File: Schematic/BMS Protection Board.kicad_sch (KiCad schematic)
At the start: 292 parts, among them J5 Conn_01x04, J6 Conn_01x04, J7 USB_C_Receptacle_USB2.0_14P, Q1 DMN2004K, Q10 ZXMP10A13F, Q11 BSS123, Q12 ZXMP10A13F, Q13 BSS123, Q14 BCX56, Q2 DMN2004K, Q3 DMN2004K, Q4 CSD19531Q5A, Q5 CSD19531Q5A, Q6 ZXMP10A13F, Q7 CSD19531Q5A, Q8 CSD19531Q5A, Q9 BSS123, SW2 SW_Push, U1 1043, U10 TVS2200DRV, U11 BQ76200PW, U12 TLV75533PDBV, U13 BQ78350DBT-R1A, U14 TPD1E05U06DYA, U15 TPD1E05U06DYA, U16 BQ25798RQMR, U2 1043, U22 1043, U23 1043, U24 1043, U25 1043, U26 1043, U27 1043, U28 TPS566238PRQFR, U3 1043, U4 1043, U5 1043, U6 1043, U7 CAT24C512WI-GT3, U8 BQ7692000PWR, U9 TPS25751DREFR

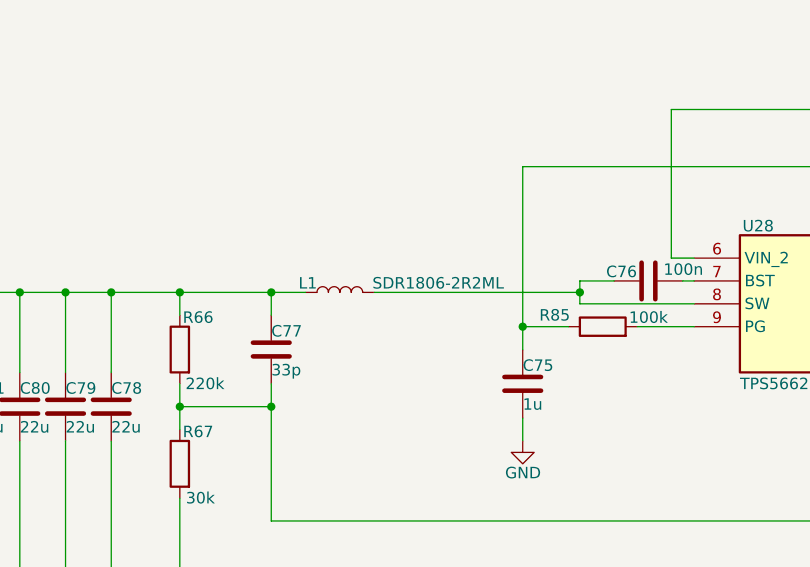
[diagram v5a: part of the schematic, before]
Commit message: Added 6V Line
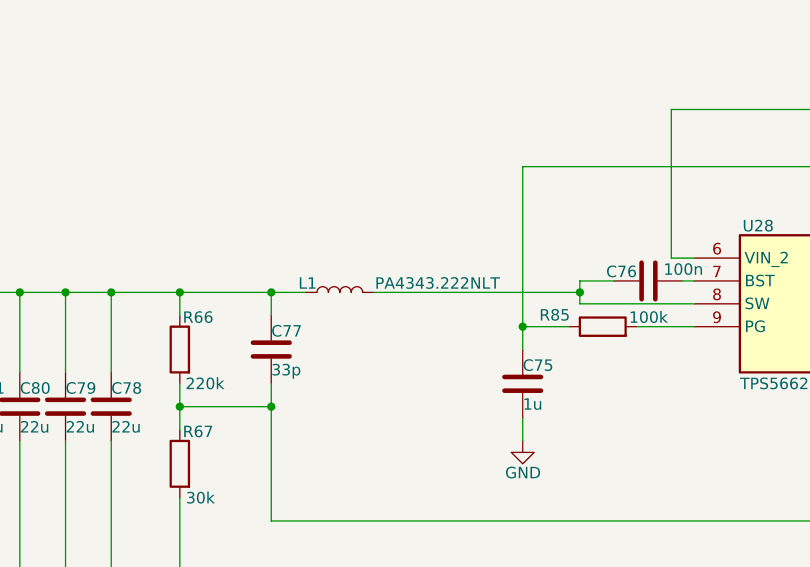
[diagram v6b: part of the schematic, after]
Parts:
- removed L1: SDR1806-2R2ML, SDR1806-2R2ML:SDR18062R2ML, symbol SDR1806-2R2ML:SDR1806-2R2ML
- added L1: PA4343.222NLT, INDPM135125X650N, symbol PA4343.222NLT:PA4343.222NLT
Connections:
- net P5V0: now also L1.1
- net at C76.1, U28.8 (SW): now also L1.2
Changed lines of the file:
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@@
 	)
 	(symbol
-		(lib_id "SDR1806-2R2ML:SDR1806-2R2ML")
-		(at 438.785 412.115 0)
-		(unit 1)
-		(exclude_from_sim no)
-		(in_bom yes)
-		(on_board yes)
-		(dnp no)
-		(property "Reference" "L1"
-			(at 440.944 411.734 0)
-			(effects
-				(font
-					(size 1.27 1.27)
-				)
-			)
-		)
-		(property "Value" "SDR1806-2R2ML"
-			(at 455.422 411.734 0)
-			(effects
-				(font
-					(size 1.27 1.27)
-				)
-			)
-		)
-		(property "Footprint" "SDR1806-2R2ML:SDR18062R2ML"
-			(at 455.295 508.305 0)
-			(effects
-				(font
-					(size 1.27 1.27)
-				)
-				(justify left top)
-				(hide yes)
-			)
-		)
-		(property "Datasheet" "https://www.bourns.com/docs/Product-Datasheets/SDR1806.pdf"
-			(at 455.295 608.305 0)
-			(effects
-				(font
-					(size 1.27 1.27)
-				)
-				(justify left top)
-				(hide yes)
-			)
-		)
-		(property "Description" "Power Inductors - SMD 2.2uH 20% SMD 1806"
-			(at 438.785 412.115 0)
-			(effects
-				(font
-					(size 1.27 1.27)
-				)
-				(hide yes)
-			)
-		)
-		(property "Height" "6.9"
-			(at 455.295 808.305 0)
-			(effects
-				(font
-					(size 1.27 1.27)
-				)
-				(justify left top)
-				(hide yes)
-			)
-		)
-		(property "Mouser Part Number" "652-SDR1806-2R2ML"
-			(at 455.295 908.305 0)
-			(effects
-				(font
-					(size 1.27 1.27)
-				)
-				(justify left top)
-				(hide yes)
-			)
-		)
-		(property "Mouser Price/Stock" "https://www.mouser.co.uk/ProductDetail/Bourns/SDR1806-2R2ML?qs=xrpI9KL%2FXvsM6NNo6hRSNQ%3D%3D"
-			(at 455.295 1008.305 0)
-			(effects
-				(font
-					(size 1.27 1.27)
-				)
-				(justify left top)
-				(hide yes)
-			)
-		)
-		(property "Manufacturer_Name" "Bourns"
-			(at 455.295 1108.305 0)
-			(effects
-				(font
-					(size 1.27 1.27)
-				)
-				(justify left top)
-				(hide yes)
-			)
-		)
-		(property "Manufacturer_Part_Number" "SDR1806-2R2ML"
-			(at 455.295 1208.305 0)
-			(effects
-				(font
-					(size 1.27 1.27)
-				)
-				(justify left top)
-				(hide yes)
-			)
-		)
-		(property "Availability" ""
-			(at 438.785 412.115 0)
-			(effects
-				(font
-					(size 1.27 1.27)
-				)
-				(hide yes)
-			)
-		)
-		(property "Check_prices" ""
-			(at 438.785 412.115 0)
-			(effects
-				(font
-					(size 1.27 1.27)
-				)
-				(hide yes)
-			)
-		)
-		(property "Description_1" ""
-			(at 438.785 412.115 0)
-			(effects
-				(font
-					(size 1.27 1.27)
-				)
-				(hide yes)
-			)
-		)
-		(property "MANUFACTURER" ""
-			(at 438.785 412.115 0)
-			(effects
-				(font
-					(size 1.27 1.27)
-				)
-				(hide yes)
-			)
-		)
-		(property "MAXIMUM_PACKAGE_HEIGHT" ""
-			(at 438.785 412.115 0)
-			(effects
-				(font
-					(size 1.27 1.27)
-				)
-				(hide yes)
-			)
-		)
-		(property "MF" ""
-			(at 438.785 412.115 0)
-			(effects
-				(font
-					(size 1.27 1.27)
-				)
-				(hide yes)
-			)
-		)
-		(property "MP" ""
-			(at 438.785 412.115 0)
-			(effects
-				(font
-					(size 1.27 1.27)
-				)
-				(hide yes)
-			)
-		)
-		(property "PARTREV" ""
-			(at 438.785 412.115 0)
-			(effects
-				(font
-					(size 1.27 1.27)
-				)
-				(hide yes)
-			)
-		)
-		(property "Package" ""
-			(at 438.785 412.115 0)
-			(effects
-				(font
-					(size 1.27 1.27)
-				)
-				(hide yes)
-			)
-		)
-		(property "Part Number" ""
-			(at 438.785 412.115 0)
-			(effects
-				(font
-					(size 1.27 1.27)
-				)
-				(hide yes)
-			)
-		)
-		(property "STANDARD" ""
-			(at 438.785 412.115 0)
-			(effects
-				(font
-					(size 1.27 1.27)
-				)
-				(hide yes)
-			)
-		)
-		(property "SnapEDA_Link" ""
-			(at 438.785 412.115 0)
-			(effects
-				(font
-					(size 1.27 1.27)
-				)
-				(hide yes)
-			)
-		)
-		(property "Specifications" ""
-			(at 438.785 412.115 0)
-			(effects
-				(font
-					(size 1.27 1.27)
-				)
-				(hide yes)
-			)
-		)
-		(pin "1"
-		)
-		(pin "2"
-		)
-		(instances
-			(project ""
-				(path "/fc8533bc-25dd-4c20-9b4c-ffebebd6739b/e8da5d81-614b-4fe5-84b3-4c351fab7114"
-					(reference "L1")
-					(unit 1)
-				)
-			)
-		)
-	)
-	(symbol
 		(lib_id "Device:R")
 		(at 135.89 168.91 90)
@@
 					(unit 1)
 				)
+			)
+		)
+	)
+	(symbol
+		(lib_id "PA4343.222NLT:PA4343.222NLT")
+		(at 444.5 412.75 90)
+		(unit 1)
+		(exclude_from_sim no)
+		(in_bom yes)
+		(on_board yes)
+		(dnp no)
+		(property "Reference" "L1"
+			(at 441.96 412.496 90)
+			(effects
+				(font
+					(size 1.27 1.27)
+				)
+				(justify left top)
+			)
+		)
+		(property "Value" "PA4343.222NLT"
+			(at 462.28 412.496 90)
+			(effects
+				(font
+					(size 1.27 1.27)
+				)
+				(justify left top)
+			)
+		)
+		(property "Footprint" "INDPM135125X650N"
+			(at 540.69 396.24 0)
+			(effects
+				(font
+					(size 1.27 1.27)
+				)
+				(justify left top)
+				(hide yes)
+			)
+		)
+		(property "Datasheet" "https://productfinder.pulseelectronics.com/api/open/part-attachments/datasheet/PA4343.222NLT"
+			(at 640.69 396.24 0)
+			(effects
+				(font
+					(size 1.27 1.27)
+				)
+				(justify left top)
+				(hide yes)
+			)
+		)
+		(property "Description" "Power Inductors - SMD 2.2uH 22A 6.5mm 20% Low Prof"
+			(at 444.5 412.75 0)
+			(effects
+				(font
+					(size 1.27 1.27)
+				)
+				(hide yes)
+			)
+		)
+		(property "Height" "6.5"
+			(at 840.69 396.24 0)
+			(effects
+				(font
+					(size 1.27 1.27)
+				)
+				(justify left top)
+				(hide yes)
+			)
+		)
+		(property "Mouser Part Number" "673-PA4343.222NLT"
+			(at 940.69 396.24 0)
+			(effects
+				(font
+					(size 1.27 1.27)
+				)
+				(justify left top)
+				(hide yes)
+			)
+		)
+		(property "Mouser Price/Stock" "https://www.mouser.co.uk/ProductDetail/Pulse-Electronics/PA4343222NLT?qs=%2FzQKu7YvIMbh7iiJmyUwAg%3D%3D"
+			(at 1040.69 396.24 0)
+			(effects
+				(font
+					(size 1.27 1.27)
+				)
+				(justify left top)
+				(hide yes)
+			)
+		)
+		(property "Manufacturer_Name" "PULSE"
+			(at 1140.69 396.24 0)
+			(effects
+				(font
+					(size 1.27 1.27)
+				)
+				(justify left top)
+				(hide yes)
+			)
+		)
+		(property "Manufacturer_Part_Number" "PA4343.222NLT"
+			(at 1240.69 396.24 0)
+			(effects
+				(font
+					(size 1.27 1.27)
+				)
+				(justify left top)
+				(hide yes)
+			)
+		)
+		(pin "1"
+		)
+		(pin "2"
+		)
+		(instances
+			(project ""
+				(path "/fc8533bc-25dd-4c20-9b4c-ffebebd6739b/e8da5d81-614b-4fe5-84b3-4c351fab7114"
+					(reference "L1")
+					(unit 1)
+				)

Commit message: bom progress
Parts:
- added SW1: SW_DPST, symbol Switch:SW_DPST
- U22, U23, U24, U25, U26, U27: now not fitted
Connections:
- net BATT+: now also SW1.4; no longer C17.1, D1.2, D17.1 (K), D8.2 (A), Q12.2 (S), R15.1, R19.1, R48.2, R7.2, R71.2, U1.1 (+), U22.1 (+), U25.1 (+), U4.1 (+)
- net BATT-: now also SW1.2; no longer D6.2 (A), Q3.2 (S), R14.1, U24.2 (-), U27.2 (-), U3.2 (-), U6.2 (-)
- new net C0: D6.2 (A), Q3.2 (S), R14.1, SW1.1, U24.2 (-), U27.2 (-), U3.2 (-), U6.2 (-)
- new net C3: C17.1, D1.2, D17.1 (K), D8.2 (A), Q12.2 (S), R15.1, R19.1, R48.2, R7.2, R71.2, SW1.3, U1.1 (+), U22.1 (+), U25.1 (+), U4.1 (+)
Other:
- note added: "BMS Protection Board for 3S Battery Pack In/Out: min voltage: 9.6 V, nominal voltage: 11.1 V, max voltage: 12.6 V Output: 25A continuous discharge current Min Each Cell set to 3.2 V, Max Each Cell set to 4.2 V"
- note added: "ICIN(rms) = Iout * sqrt((Vout / Vin_min) * ((Vin_min - Vout) / Vin_min)) ICIN(rms) = 5A * sqrt((5V / 9V) * ((9V - 5V) / 9V)) = 2.48A"
- note added: "I_L(ripple) = (Vout * (Vin_max - Vout)) / (Vin_max * Lout * Fsw) I_L(ripple) = (5 * (12.6 - 5)) / (12.6 * 2.2u * 594130) = 2.31A"
- note added: "VSYS caps need 2A ripple support"
- note removed: "BMS Protection Board for 3S4P Battery Pack In/Out: min voltage: 9.6 V, nominal voltage: 11.1 V, max voltage: 12.6 V Output: 25A continuous discharge current Min Each Cell set to 3.2 V, Max Each Cell set to 4.2 V"

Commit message: 100n cap
100n cap bom
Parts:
- C11, C12, C13, C14, C22, C24, C25, C33, C37, C41, C44, C5, C55, C58, C59, C60, C62, C7, C76, C8, C82, C83, C86, C92, C96: footprint (none) -> CL10B104MB8NNNC:CAPC1608X90N; Link (none) -> https://mou.sr/3JWJm45; Manufacturer Part Number (none) -> CL10B104MB8NNNC; Price per Unit (none) -> 0.10; Supplier (none) -> Mouser; Supplier Part Number (none) -> 187-CL10B104MB8NNNC
